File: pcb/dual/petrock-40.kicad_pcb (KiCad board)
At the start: 2 copper layers, 242.5 x 87.9 mm, 100 parts, among them J1 MJ-4PP-9, J2 OLED, J3 MJ-4PP-9, J4 OLED, SW1 SW_PUSH, SW10 SW_PUSH, SW11 SW_PUSH, SW12 SW_PUSH, SW13 SW_PUSH, SW14 SW_PUSH, SW15 SW_PUSH, SW16 SW_PUSH, SW17 SW_PUSH, SW18 SW_PUSH, SW2 SW_PUSH, SW20 SW_PUSH, SW21 SW_PUSH, SW22 SW_PUSH, SW23 SW_PUSH, SW24 SW_PUSH, SW25 SW_PUSH, SW26 SW_PUSH, SW27 SW_PUSH, SW29 SW_PUSH, SW3 SW_PUSH, SW30 SW_PUSH, SW31 SW_PUSH, SW32 SW_PUSH, SW33 SW_PUSH, SW34 SW_PUSH, SW35 SW_PUSH, SW36 SW_PUSH, SW37 SW_PUSH, SW38 SW_PUSH, SW39 SW_PUSH, SW4 SW_PUSH, SW41 SW_PUSH, SW42 SW_PUSH, SW43 SW_PUSH, SW44 SW_PUSH, SW5 SW_PUSH, SW6 SW_PUSH, SW8 SW_PUSH, SW9 SW_PUSH, U1 ProMicro, U2 ProMicro

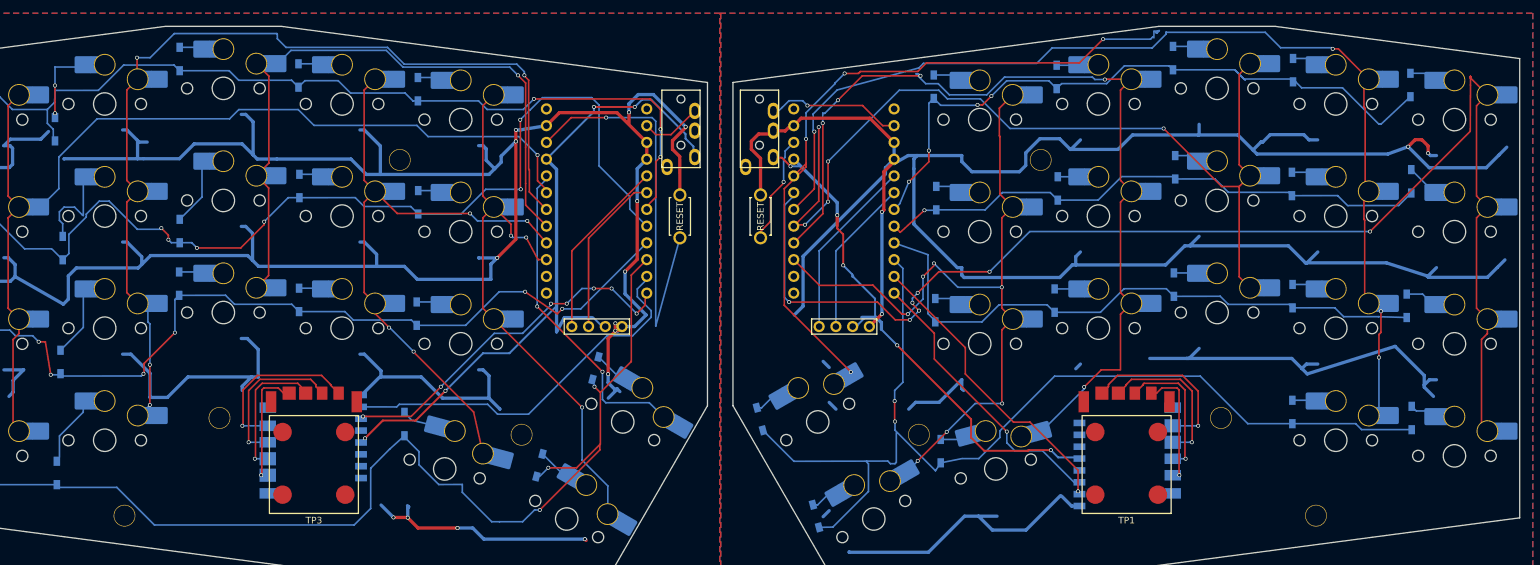
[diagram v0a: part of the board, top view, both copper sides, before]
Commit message: Wireless-ready pins, last-resort routing, fresh renders
The trackpoint moves to controller pins 1/2 (a nice!nano's high-frequency
D1/D0, as the ZMK PS/2 driver recommends) and each TRRS data line to pin
11 (tools/pins.py); wired QMK on an RP2040 handles both. A connection
boxed in by stock copper may now rip it up as a last resort, so both
boards route fully. README documents the wired and wireless pinouts.
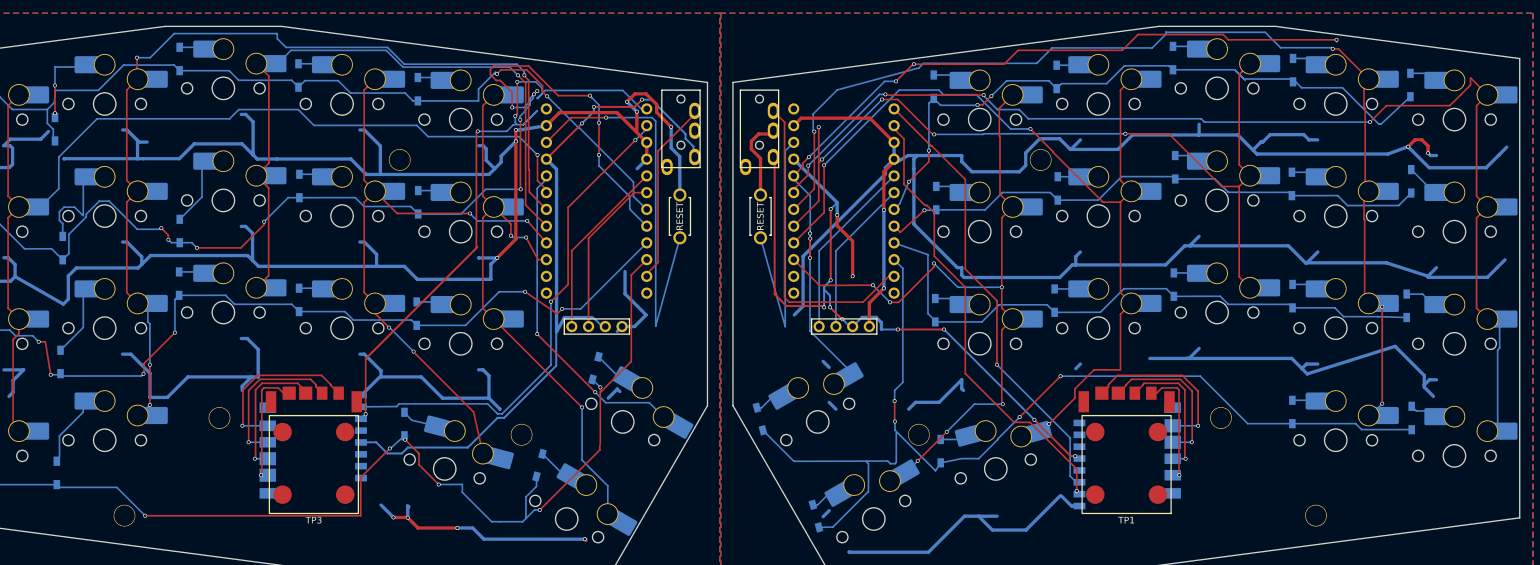
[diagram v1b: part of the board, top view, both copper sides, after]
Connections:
- U1 pad 1: (no net) -> TP_CLK_L
- U1 pad 11: TP_DATA_L -> data
- U1 pad 12: TP_CLK_L -> unconnected-(U1-9/B5-Pad12)
- U1 pad 2: data -> TP_DATA_L
- U2 pad 1: (no net) -> TP_CLK
- U2 pad 11: TP_DATA -> data_r
- U2 pad 12: TP_CLK -> unconnected-(U2-9/B5-Pad12)
- U2 pad 2: data_r -> TP_DATA
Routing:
- net TP_CLK_L: track 54.5 -> 118.0 mm, vias 7 -> 4
- net col1_r: track 201.6 -> 170.7 mm, vias 7 -> 4
- net VDD: track 88.0 -> 116.9 mm, vias 5 -> 11
- net GND: track 478.0 -> 449.2 mm, vias 14 -> 10
- net reset_r: track 15.6 -> 42.5 mm, vias 1 -> 0
- net data_r: track 21.1 -> 46.7 mm, vias 1 -> 0
- net TP_CLK: track 42.5 -> 67.7 mm
- net row1: track 151.0 -> 174.9 mm, vias 6 -> 12
- net TP_DATA: track 45.6 -> 68.5 mm
- net col0_r: track 107.8 -> 128.6 mm, vias 4 -> 7
- net data: track 9.25 -> 26.9 mm
- net TP_DATA_L: track 57.7 -> 74.2 mm, vias 0 -> 2
- net col3_r: track 138.6 -> 126.9 mm
- net row0: track 137.9 -> 132.7 mm, vias 3 -> 2
- net row3: track 167.2 -> 162.6 mm, vias 3 -> 6
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
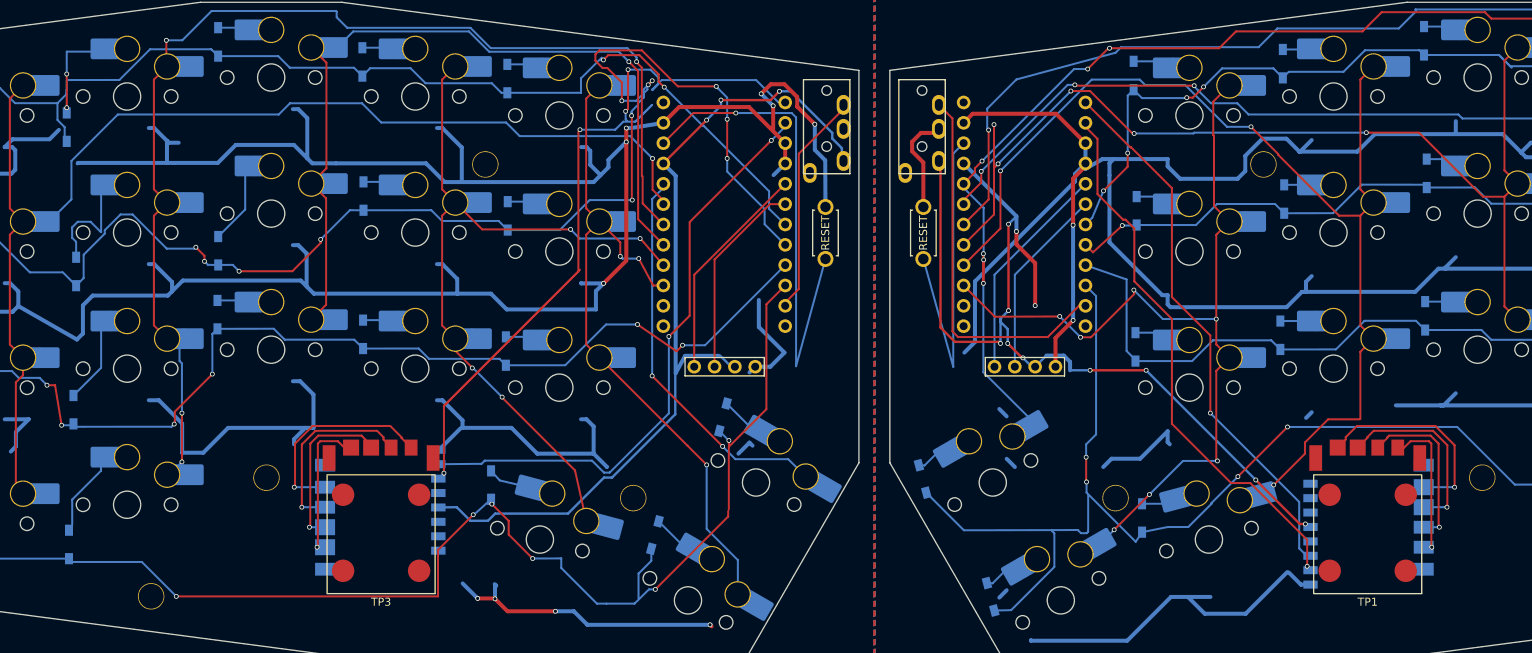
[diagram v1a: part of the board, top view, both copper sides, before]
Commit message: Hand-solder gaps of 0.9 mm, pinned tools, clean pours
Every hand-soldered pad now leaves at least 0.9 mm to the next (headers
stay at the standard 2.54 mm pitch): trackpoint sensor-link pads 1.6 mm
wide, driver host pads 0.9 mm, TRRS slot pads 2.1 mm long.

Pours drop floating islands. The last-resort routing pass repeats until
nothing is open. KiCad, Python and friends are pinned as GC roots in
.nix/ (bin/setup), so garbage collection can't break the build again.
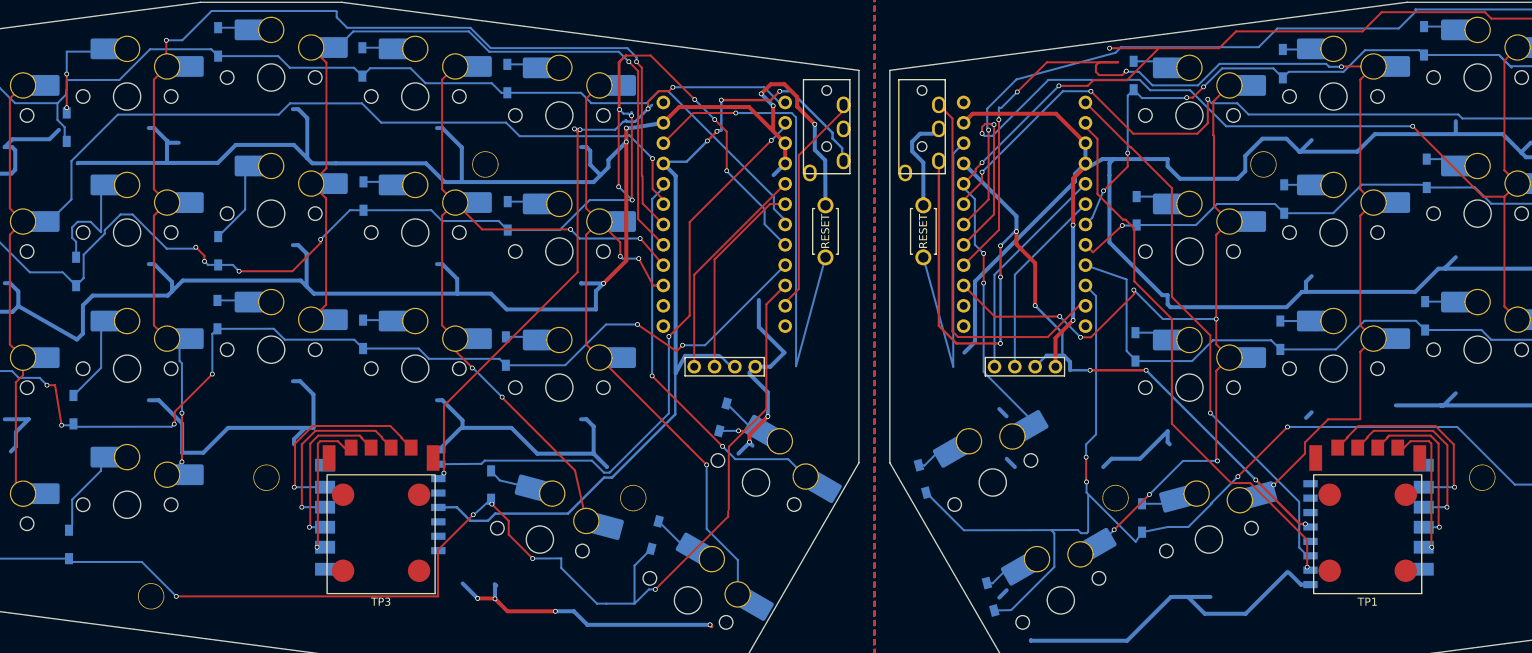
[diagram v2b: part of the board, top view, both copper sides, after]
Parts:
- moved RSW2 0.20 mm to (162.0, 80.4)
- moved RSW1 0.20 mm to (149.7, 80.4)
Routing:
- net TP_CLK_L: track 118.0 -> 92.2 mm, vias 4 -> 5
- net GND: track 449.2 -> 459.5 mm, vias 10 -> 12
- net col4_r: track 134.3 -> 143.8 mm, vias 3 -> 5
- net row0: track 132.7 -> 127.2 mm, vias 2 -> 0
- net col1_r: track 170.7 -> 175.0 mm
- net col3_r: track 126.9 -> 130.3 mm, vias 5 -> 3
- net row1: track 174.9 -> 178.3 mm, vias 12 -> 11
- net col0_r: track 128.6 -> 131.0 mm, vias 7 -> 6
- net VCC: track 106.2 -> 108.4 mm, vias 3 -> 4
- net row3: track 162.6 -> 163.5 mm
- net VDD: track 116.9 -> 116.4 mm, vias 11 -> 9

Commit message: Trackpoint driver host pads that fit both the drawing and the real board
The datasheet's 3.08 mm runs to pin 1's pad edge, not its centre, and its
1.80 mm pitch disagrees with holykeebs' photos of the Rev A board (1.72 mm,
scale-checked against the 2.5 mm link pads). Both agree on the row's middle,
so the host pads now sit at 1.758 mm pitch about it: every pin within 0.20 mm
of its pad's centre whichever is right. Pads 0.85 mm wide, gaps 0.9 mm.
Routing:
- net col0_r: track 131.0 -> 82.9 mm, vias 6 -> 5
- net VDD: track 116.4 -> 134.9 mm, vias 9 -> 7
- net col1_r: track 175.0 -> 192.8 mm
- net GND: track 459.5 -> 469.9 mm, vias 12 -> 13
- net col3_r: track 130.3 -> 136.9 mm, vias 3 -> 5
- net col4_r: track 143.8 -> 140.3 mm, vias 5 -> 7
- net VCC: track 108.4 -> 106.8 mm
- net row1: track 178.3 -> 177.6 mm, vias 11 -> 8
- net TP_CLK_L: track 92.2 -> 92.7 mm
- net TP_CLK: track 67.6 -> 67.1 mm

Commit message: Evenly spaced controller corner with exact nice!nano and jack sizes
Keycap, controller, jack and edge now sit 1.63 mm apart, and the
controller's and jack's square top corners are 1.15 mm inside the slope,
square to it, like the keycaps. Sizes come from 3D models: the nice!nano's
board is 17.78 x 33.0 mm with its USB end 3.79 mm past the first pin; the
PJ320A body is 6.0 mm. The render stand-in controller now has those sizes.
drop_dangling also catches lengths DRC prints in exponent form.
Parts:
- moved J2 1.36 mm to (132.0, 97.0)
- moved U1 1.36 mm to (135.8, 78.5)
- moved J4 1.36 mm to (172.2, 97.0)
- moved U2 1.36 mm to (175.9, 78.5)
- moved J3 0.61 mm to (162.4, 61.2)
- moved J1 0.61 mm to (149.3, 61.2)
- moved RSW1 0.46 mm to (149.3, 80.3)
- moved RSW2 0.45 mm to (162.4, 80.3)
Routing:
- net col0: track 48.2 -> 157.4 mm, vias 2 -> 9
- net col1: track 146.7 -> 245.4 mm, vias 1 -> 12
- net GND: track 469.9 -> 415.5 mm, vias 13 -> 9
- net GNDA: track 446.7 -> 488.1 mm, vias 4 -> 5
- net VCC: track 106.8 -> 145.4 mm, vias 4 -> 6
- net col0_r: track 82.9 -> 52.6 mm
- net VDD: track 134.9 -> 107.2 mm, vias 7 -> 10
- net row1: track 177.6 -> 151.7 mm, vias 8 -> 10
- net row0: track 127.2 -> 148.0 mm, vias 0 -> 2
- net data: track 27.0 -> 40.9 mm, vias 0 -> 1
- net col3_r: track 136.9 -> 126.0 mm
- net TP_CLK_L: track 92.7 -> 84.8 mm, vias 5 -> 2
- net col1_r: track 192.8 -> 186.5 mm
- net row3: track 163.5 -> 169.6 mm, vias 6 -> 3
- net col2: track 141.3 -> 146.0 mm, vias 4 -> 7
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
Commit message: Five standoffs per half, logo on the board, plain controller corner
The standoff the outer pinky column lost moves to where the pinky and ring
columns meet, so the outer top corner is supported again (10 in all). The
logo is back on the board's silkscreen. The jack, reset button and OLED
header lose their printed outlines. The plate's opening by the controller
now starts at the inner index keycap line instead of the stock plate's
fixed edge, clearing the moved controller's sockets by 1.66 mm. The board
records its ENIG finish; renders can hide the jack and reset ("wireless").
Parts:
- added h2: h2, holykeebs:M2_SPACER, F.Cu at (53.8, 73.0)
- added h2: h2, holykeebs:M2_SPACER, B.Cu at (258.0, 73.0)
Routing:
- net col1: track 245.4 -> 148.4 mm, vias 12 -> 2
- net col0_r: track 52.6 -> 131.0 mm, vias 5 -> 10
- net GND: track 415.5 -> 465.1 mm, vias 9 -> 12
- net GNDA: track 488.1 -> 465.0 mm
- net VCC: track 145.4 -> 161.3 mm
- net row0: track 148.0 -> 135.6 mm
- net row1: track 151.7 -> 161.9 mm, vias 10 -> 8
- net col0: track 157.4 -> 150.4 mm
- net col3: track 104.3 -> 98.8 mm, vias 4 -> 1
- net col1_r: track 186.5 -> 181.0 mm, vias 4 -> 6
- net col2: track 146.0 -> 148.5 mm
- net TP_CLK_L: track 84.8 -> 86.3 mm
- net row3: track 169.6 -> 168.8 mm
- net col5: track 84.3 -> 84.1 mm, vias 7 -> 3

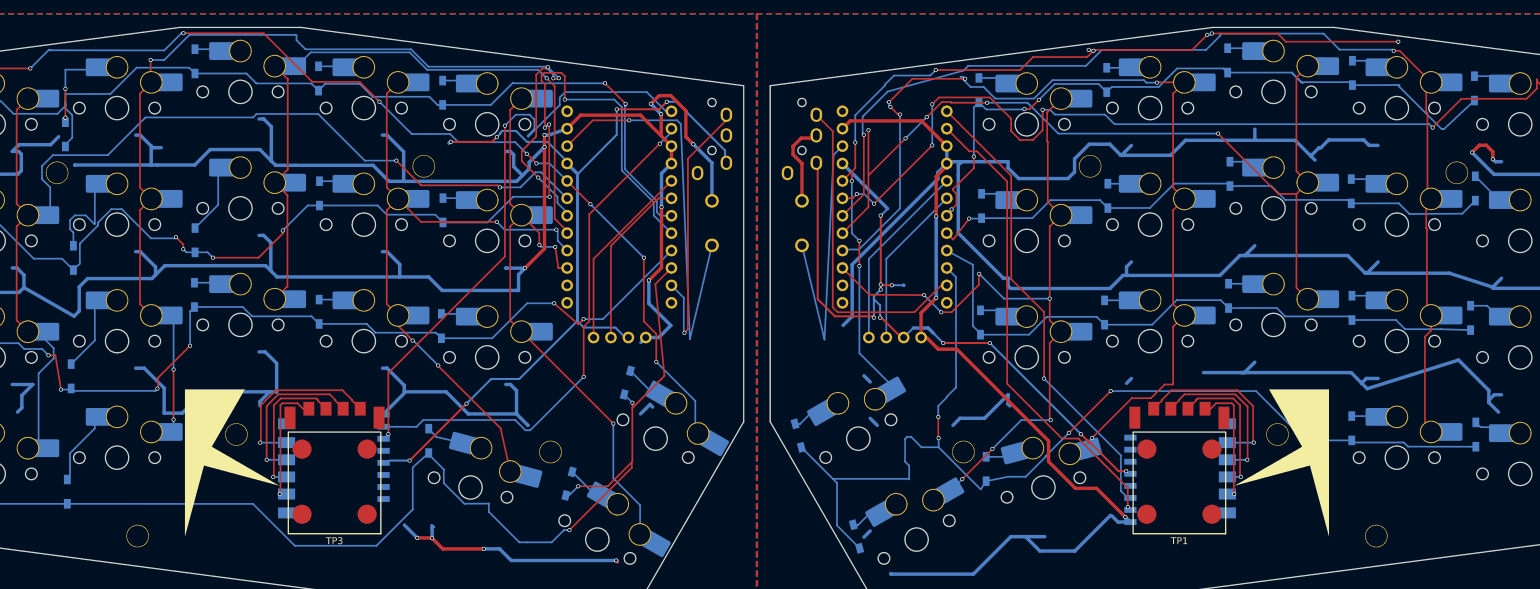
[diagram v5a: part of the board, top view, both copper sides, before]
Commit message: Standoffs placed by geometry
Each standoff between four keys sits at the four keys' centre (midway
between the columns and between their staggered row gaps): pinky and
ring top and bottom, index and inner index at the top. The thumb one
is equally far from its three keycap corners, and the one by the
trackpoint sits at the centre of the key cell the logo's notch outlines.
D29 moves 0.3 mm to make room and stays clear. Standoffs keep 1.5 mm
from the logo.
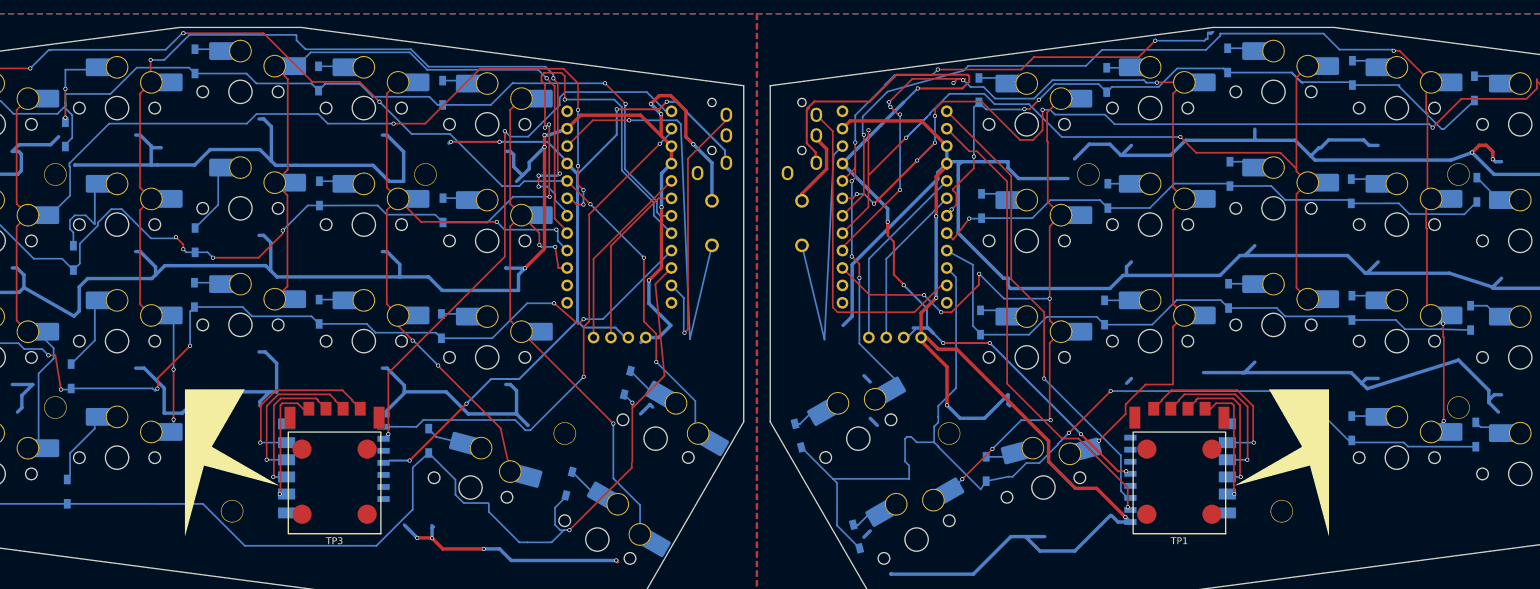
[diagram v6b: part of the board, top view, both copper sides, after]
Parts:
- moved h2 22.3 mm to (53.5, 107.2)
- moved h2 22.3 mm to (258.2, 107.2)
- moved h2 11.2 mm to (79.3, 122.4)
- moved h2 11.2 mm to (232.4, 122.4)
- moved h2 3.41 mm to (183.9, 111.0)
- moved h2 3.41 mm to (127.8, 111.0)
- moved ? 1.22 mm to (204.2, 73.2)
- moved ? 1.22 mm to (107.5, 73.2)
- moved h2 0.35 mm to (53.5, 73.2)
- moved h2 0.35 mm to (258.2, 73.2)
- moved D29 0.30 mm to (260.9, 75.5)
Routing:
- net GNDA: track 465.0 -> 495.6 mm, vias 5 -> 6
- net col0_r: track 131.0 -> 102.7 mm, vias 10 -> 6
- net VDD: track 107.2 -> 131.0 mm, vias 10 -> 7
- net col1: track 148.4 -> 165.4 mm, vias 2 -> 5
- net GND: track 465.1 -> 448.7 mm
- net col1_r: track 181.0 -> 191.3 mm, vias 6 -> 7
- net TP_CLK_L: track 86.3 -> 81.1 mm
- net row3: track 168.8 -> 164.0 mm, vias 3 -> 2
- net col3_r: track 126.0 -> 129.9 mm, vias 5 -> 3
- net VCC: track 161.3 -> 159.9 mm
- net row3_r: track 158.1 -> 157.3 mm, vias 4 -> 2
- net col4_r: track 138.0 -> 138.8 mm, vias 6 -> 8
- net col2: track 148.5 -> 149.1 mm
- net col0: track 150.4 -> 150.7 mm, vias 9 -> 7
- net col2_r: track 157.3 -> 157.2 mm, vias 2 -> 4
